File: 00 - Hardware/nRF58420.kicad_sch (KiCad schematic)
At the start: 33 parts, among them IC2 E22-900M22S, J5 SMA_ST_SMD, U5 nRF52840-QFAA, Y1 Crystal

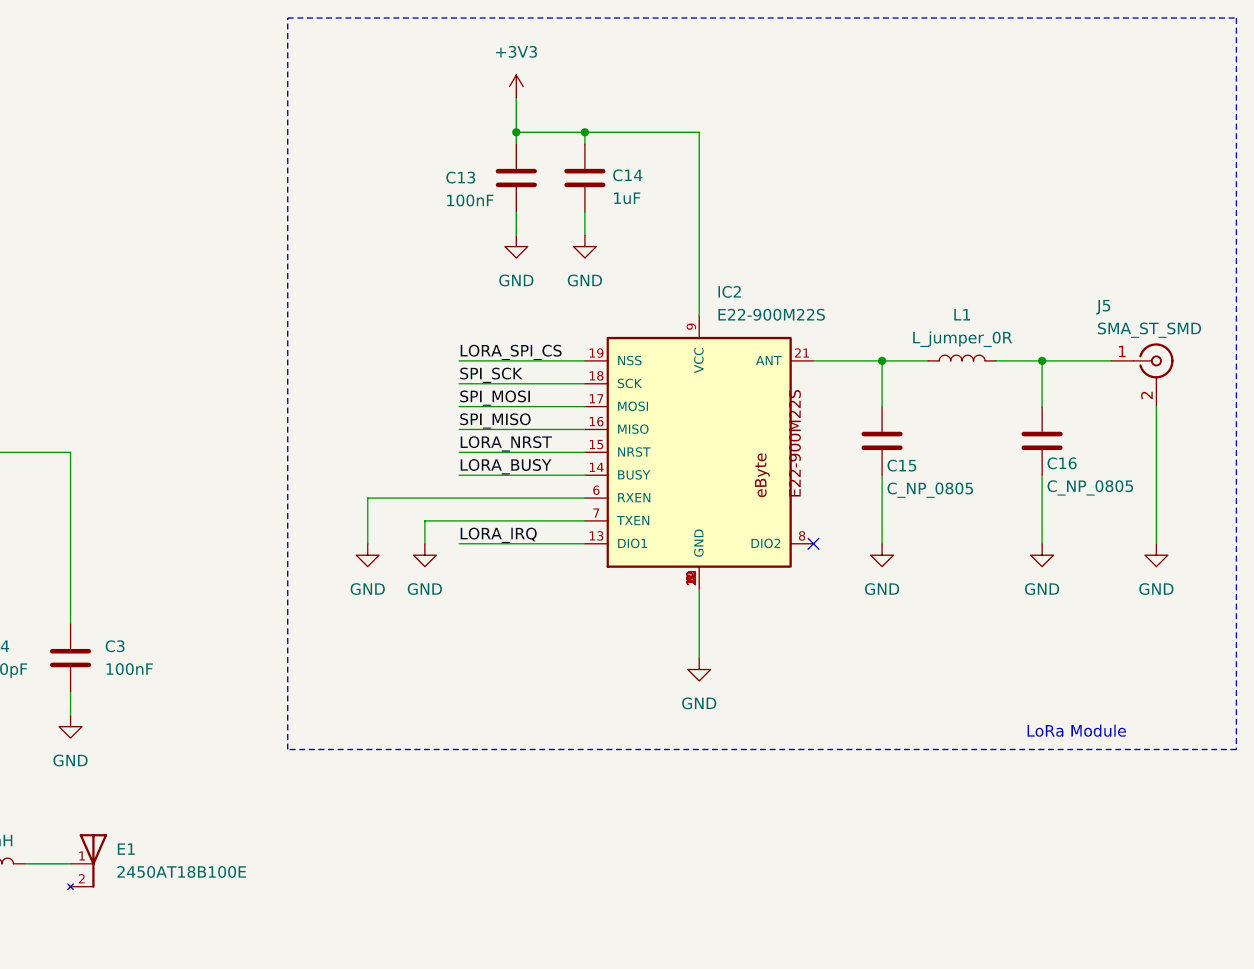
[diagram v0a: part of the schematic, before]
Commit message: updated FDTI cbus connections
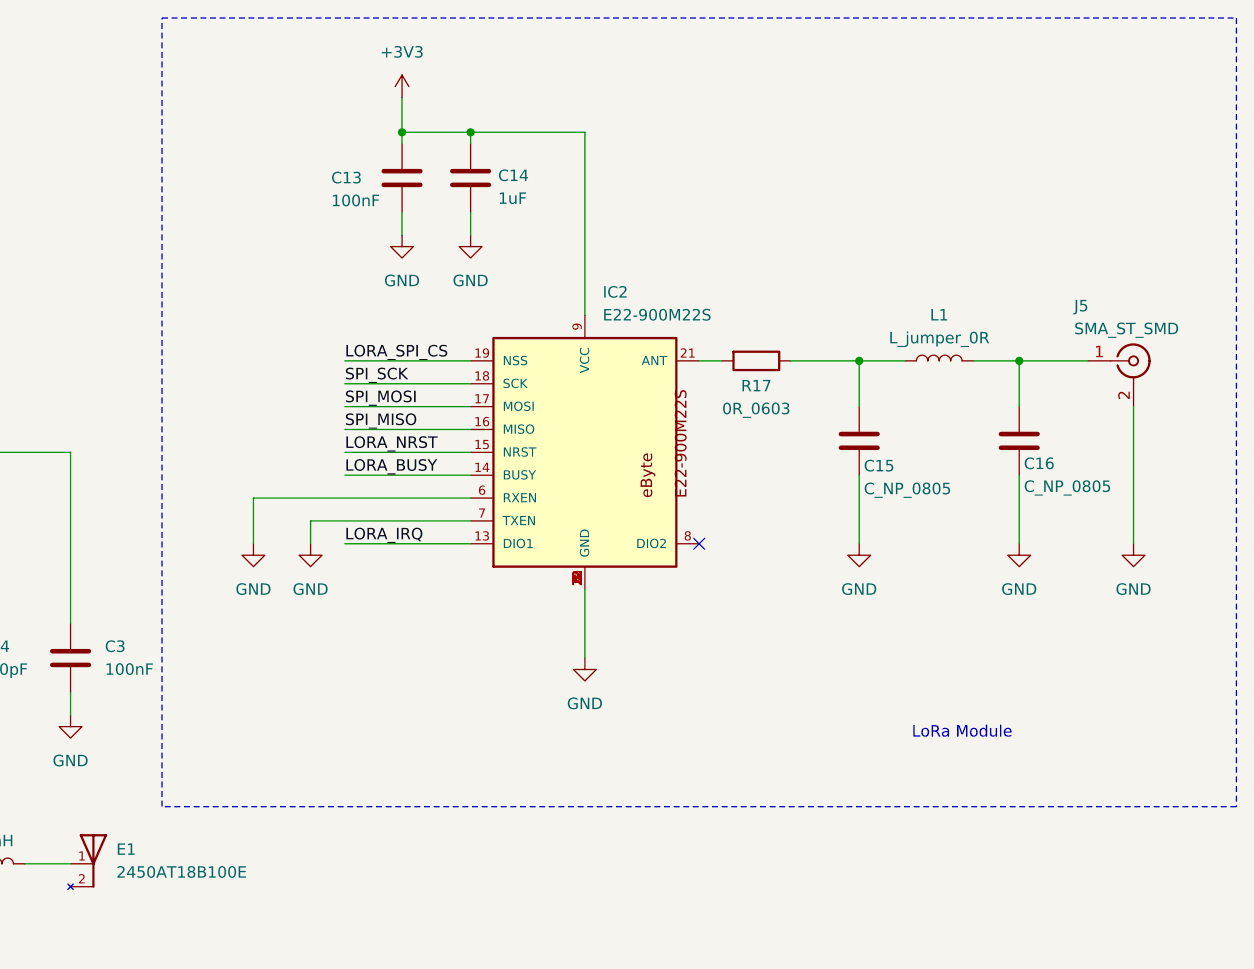
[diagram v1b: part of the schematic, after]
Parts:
- added R17: 0R_0603, Resistor_SMD:R_0603_1608Metric, symbol IBA_resistors:0R_0603
- E1: Check_prices https://www.snapeda.com/parts/2450AT18B100E/Johanson/view-p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 -> (none); Description_1 2.4GHz - Chip RF Antenna 2.4GHz ~ 2.5GHz 0.5dBi Solder Surf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 -> (none); MANUFACTURER Johanson Technology -> (none); MF Johanson Technology -> (none); MFR1 (none) -> Johanson Technology; MP 2450AT18B100E -> (none); PARTREV 4.0 -> (none); Package None -> (none); Price None -> (none); STANDARD Manufacturer Recommendation -> (none); SnapEDA_Link https://www.snapeda.com/parts/2450AT18B100E/Johanson/view-p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 -> (none)
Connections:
- net at C15.1, L1.1: now also R17.1; no longer IC2.21 (ANT)
- new net: IC2.21 (ANT), R17.2
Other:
- moved on the sheet: C13, C14, C15, C16, IC2, J5, L1
